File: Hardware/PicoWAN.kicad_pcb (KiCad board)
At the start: 2 copper layers, 50.8 x 22.9 mm, 54 parts, among them J1 Battery, J2 SWD, J3 Conn_left, J4 Conn_right, P1 USB_C_Plug_USB2.0, Q1 DMG3415U-7, U1 AP2112K-3.3, U2 RP2040, U3 MCP73831-2-OT, U4 W25Q16JV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

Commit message: add logo and labels
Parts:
- removed the G*** at (174.2, 92.7)
- added G***: LOGO, Aesthetics:electronic_cats_logo_8x6, B.Cu at (142.2, 88.9)
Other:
- board text added: "PicoWAN"
- board text added: "v1.0"

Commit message: Move_Micro
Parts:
- AE1: footprint pico-wan:SMA_EDGE -> Connectors:MOLEX_1661
- moved J2 4.42 mm to (146.4, 88.8)
- moved C8 2.92 mm to (148.2, 93.9), turned to 90 degrees
- moved D3 2.88 mm to (149.7, 89.4), turned to 90 degrees
- moved C3 2.68 mm to (153.6, 90.4)
- moved C11 2.49 mm to (154.9, 89.1)
- moved Y1 2.43 mm to (153.2, 87.1)
- moved C2 2.38 mm to (151.3, 88.2)
- moved C10 2.36 mm to (155.1, 95.5)
- moved C15 2.36 mm to (155.7, 96.2)
- moved R4 2.20 mm to (162.3, 98.6)
- moved R5 2.20 mm to (161.6, 98.0)
- moved C4 2.14 mm to (159.9, 98.7)
- moved C1 2.07 mm to (154.7, 85.4)
- moved C12 2.07 mm to (166.0, 91.1)
- moved C19 2.07 mm to (166.4, 97.8)
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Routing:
- net +3V3: track 143.7 -> 121.5 mm
- net GND: track 120.9 -> 140.8 mm, vias 17 -> 20
- net /D25: track 9.39 -> 18.2 mm
- net /D24: track 10.8 -> 19.6 mm
- net +1V2: track 22.2 -> 30.7 mm, vias 0 -> 2
- net /CIPO_0: track 14.6 -> 22.4 mm
- net /SCK_0: track 14.8 -> 22.5 mm
- net /CIPO_1: track 9.56 -> 15.1 mm
- net /RST: track 40.3 -> 34.9 mm, vias 3 -> 2
- net /SCK_1: track 13.9 -> 8.81 mm
- net /QSPI_CS: track 37.6 -> 32.5 mm
- net /RF_RST: track 16.7 -> 11.7 mm
- net /COPI_0: track 18.1 -> 23.0 mm
- net /DIO5: track 19.6 -> 15.0 mm
- net /A1: track 18.2 -> 21.1 mm
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
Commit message: Add_GND
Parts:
- moved G*** 4.89 mm to (137.6, 90.4)
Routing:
- net +3V3: track 121.5 -> 128.2 mm, vias 9 -> 8
- net GND: track 140.8 -> 135.5 mm, vias 20 -> 36
- net +1V2: track 30.7 -> 29.9 mm
- net Net-(AE1-Pad1): track 10.9 -> 10.3 mm
- net /D4: track 26.2 -> 25.6 mm

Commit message: Add_Fottprint
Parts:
- U4: footprint Package_SON:SON-8-1EP_3x2mm_P0.5mm_EP1.4x1.6mm -> hunter-cat-nfc:PSON50P200X300X50-9N
- moved U4 0.08 mm to (166.4, 95.2)
- renumbered BOOT to SW1, RST to SW2
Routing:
- net GND: track 135.5 -> 134.7 mm

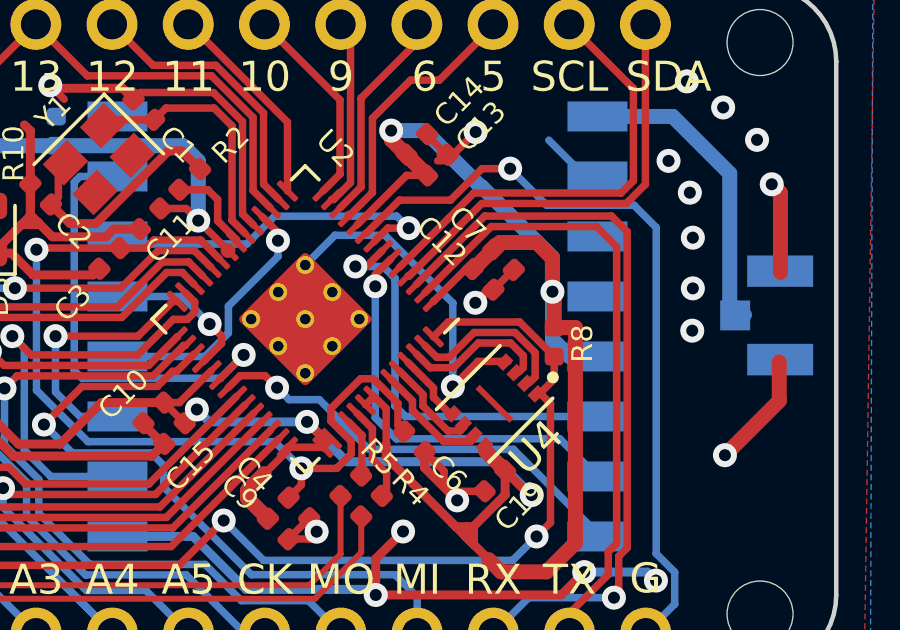
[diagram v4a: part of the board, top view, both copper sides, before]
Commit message: Add_track
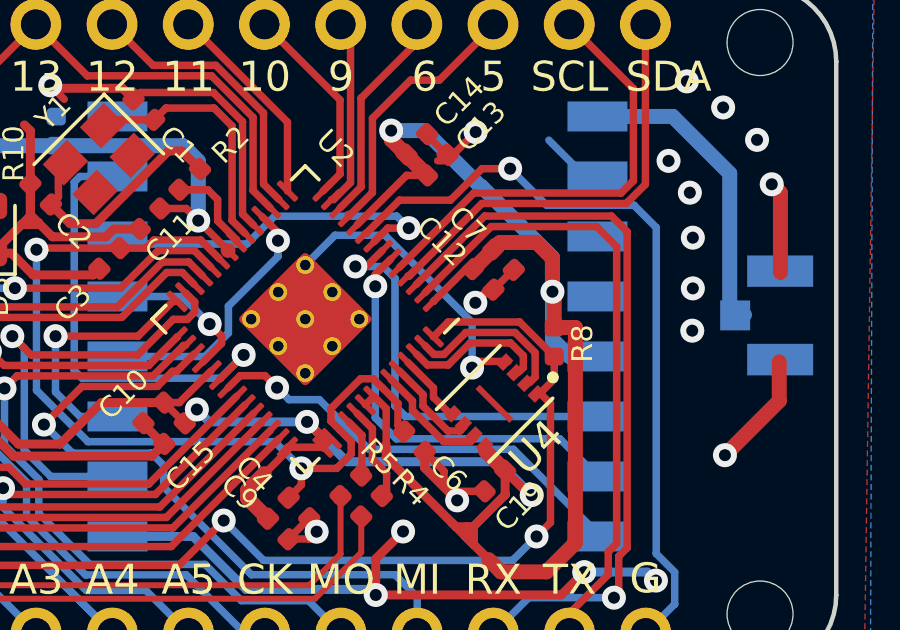
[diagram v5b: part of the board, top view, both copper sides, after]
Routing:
- net GND: track 134.7 -> 133.4 mm

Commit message: add logo front
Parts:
- added G***: LOGO, Aesthetics:electronic_cats_logo_4x3, F.Cu at (172.5, 88.6)

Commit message: Add_Labels
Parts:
- moved G*** 1.37 mm to (172.2, 90.0)
- moved C1 0.17 mm to (154.8, 85.6)
- renumbered SW1 to BOOT, SW2 to RST
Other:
- board text added: "."
- board text added: "D4"

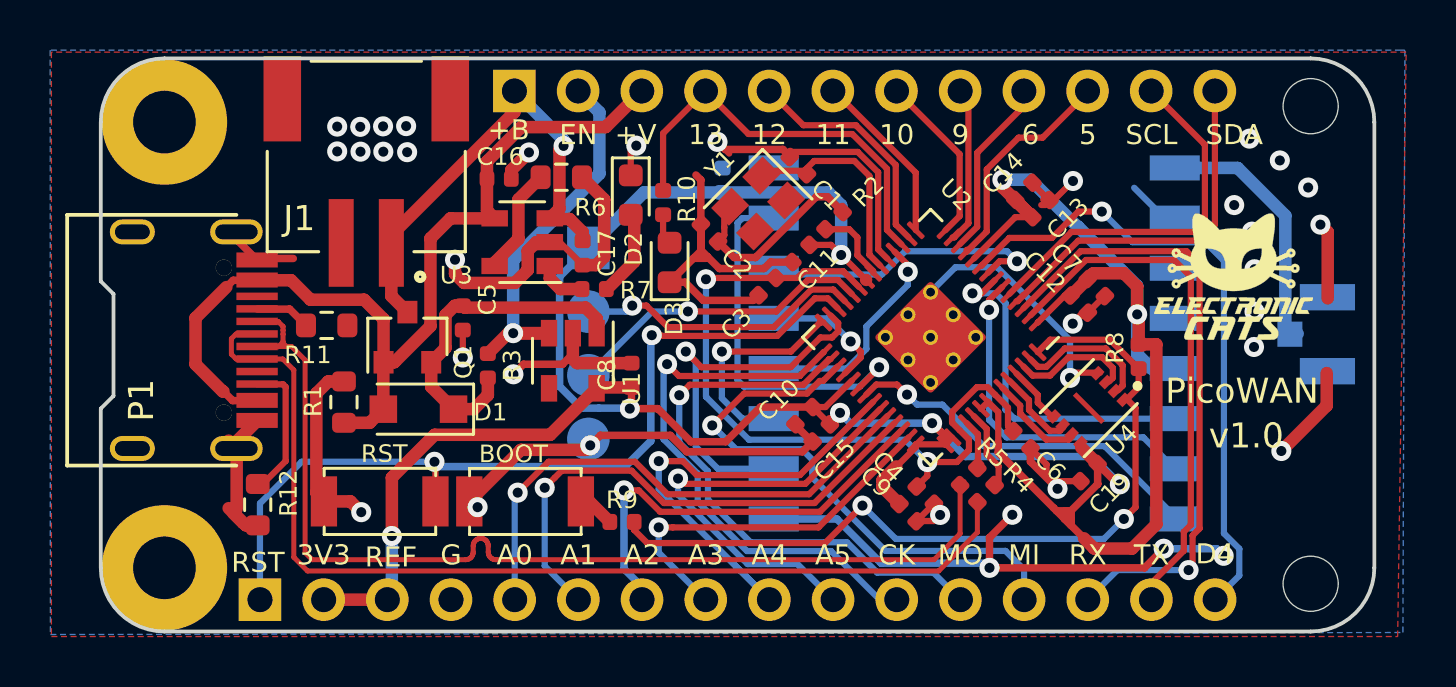
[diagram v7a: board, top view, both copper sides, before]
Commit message: fix traces
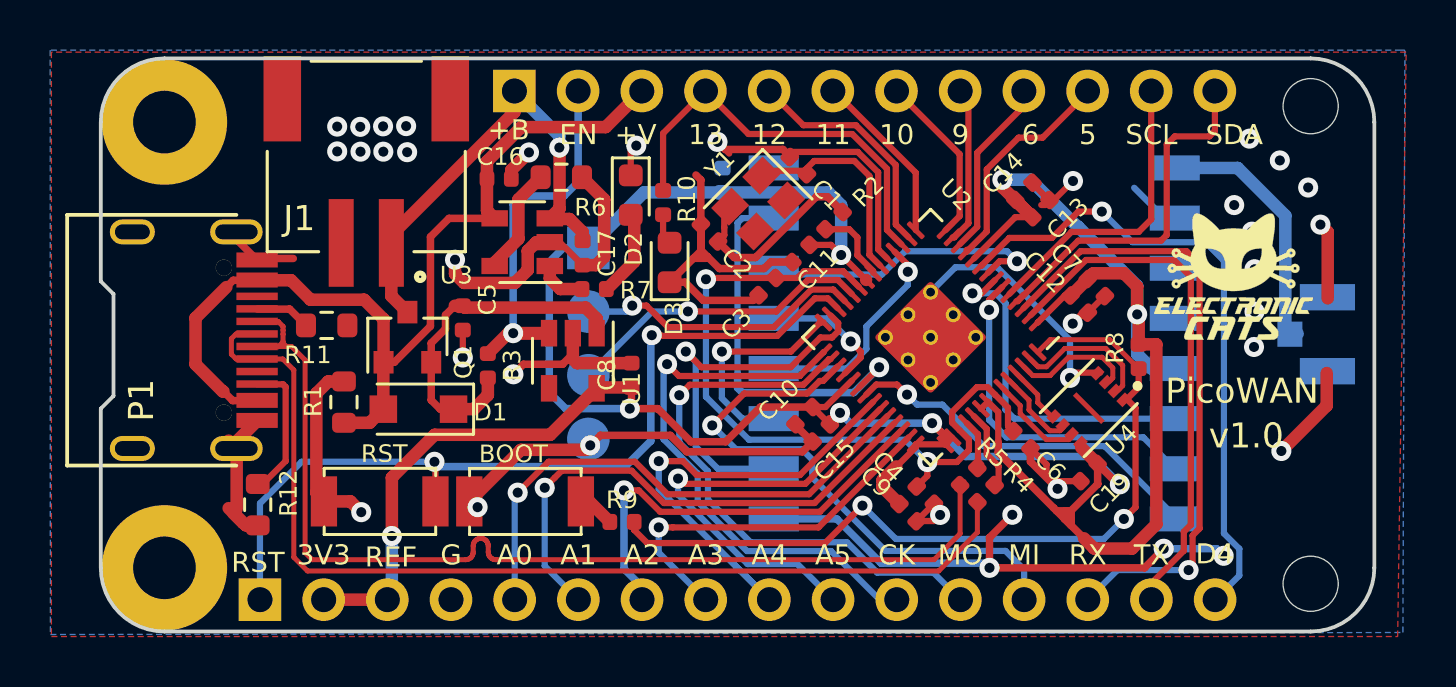
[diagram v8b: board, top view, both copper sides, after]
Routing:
- net /SCL: track 15.1 -> 12.0 mm
- net +3V3: track 128.2 -> 129.5 mm
